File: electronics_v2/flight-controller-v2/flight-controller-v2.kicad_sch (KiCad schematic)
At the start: 4 parts

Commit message: develop Hall velocity sense circuit
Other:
- sheet sensors ports: added HALL_IC; removed none
- note added: "zapasowy uart zapasowe gpio peryferium ETR/IC więcej ledów"
- note removed: "zapasowy uart zapasowe gpio hal + komperator + peryferium więcej ledów"
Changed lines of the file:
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@@
     (effects (font (size 1.27 1.27)) (justify left bottom))
   )
-  (text "zapasowy uart\nzapasowe gpio\n\nhal + komperator + peryferium\n\nwięcej ledów"
+  (text "zapasowy uart\nzapasowe gpio\n\nperyferium ETR/IC\n\nwięcej ledów"
     (at 133.35 62.23 0)
     (effects (font (size 1.27 1.27)) (justify left bottom))
@@
       (effects (font (size 1.27 1.27)) (justify left))
     )
+    (pin "HALL_IC" output (at 173.99 80.01 180)
+      (effects (font (size 1.27 1.27)) (justify left))
+    )
   )
   (sheet_instances
@@
       (reference "#PWR?") (unit 1) (value "+3.3V") (footprint "")
     )
+    (path "/d1a36df1-5a51-492c-9a9f-effbb0092bf0/20096bc6-a896-4154-a5ab-fade95ff73b7"
+      (reference "#PWR?") (unit 1) (value "+3.3V") (footprint "")
+    )
     (path "/149c5d61-baf1-4212-9ad9-405f30b44c95/21926d48-3026-48c6-8cdc-e5929b77d4ef"
       (reference "#PWR?") (unit 1) (value "+3.3V") (footprint "")
@@
       (reference "#PWR?") (unit 1) (value "+3.3V") (footprint "")
     )
+    (path "/d1a36df1-5a51-492c-9a9f-effbb0092bf0/29cb5c89-06d9-4006-9814-2a4880c1b819"
+      (reference "#PWR?") (unit 1) (value "+3.3V") (footprint "")
+    )
     (path "/149c5d61-baf1-4212-9ad9-405f30b44c95/2ece62cc-6dc1-45d6-8c6e-3513ac4effd1"
       (reference "#PWR?") (unit 1) (value "GND") (footprint "")
@@
       (reference "#PWR?") (unit 1) (value "GND") (footprint "")
     )
+    (path "/d1a36df1-5a51-492c-9a9f-effbb0092bf0/377607cf-041d-4d18-b109-f0b4ec6f876a"
+      (reference "#PWR?") (unit 1) (value "+3.3V") (footprint "")
+    )
     (path "/d1a36df1-5a51-492c-9a9f-effbb0092bf0/38858d2f-1770-4298-a4e3-3f81257a2d0d"
       (reference "#PWR?") (unit 1) (value "+3.3V") (footprint "")
@@
       (reference "#PWR?") (unit 1) (value "+3.3V") (footprint "")
     )
+    (path "/d1a36df1-5a51-492c-9a9f-effbb0092bf0/464ba5a5-93fd-41e6-84ea-ede7d22b71fe"
+      (reference "#PWR?") (unit 1) (value "+3.3V") (footprint "")
+    )
     (path "/149c5d61-baf1-4212-9ad9-405f30b44c95/4a7c64b9-2073-446f-bf89-c69240feb67e"
       (reference "#PWR?") (unit 1) (value "GND") (footprint "")
@@
       (reference "#PWR?") (unit 1) (value "GND") (footprint "")
     )
+    (path "/d1a36df1-5a51-492c-9a9f-effbb0092bf0/522011a0-f0d8-4ba7-9e6f-5ff9a33e38b1"
+      (reference "#PWR?") (unit 1) (value "GND") (footprint "")
+    )
     (path "/d1a36df1-5a51-492c-9a9f-effbb0092bf0/5d48f08e-8f67-44af-a8a7-923a56ca9605"
+      (reference "#PWR?") (unit 1) (value "GND") (footprint "")
+    )
+    (path "/d1a36df1-5a51-492c-9a9f-effbb0092bf0/5effa745-d9f7-4e5b-b649-a19cf3afaa93"
       (reference "#PWR?") (unit 1) (value "GND") (footprint "")
     )
@@
       (reference "#PWR?") (unit 1) (value "GND") (footprint "")
     )
+    (path "/d1a36df1-5a51-492c-9a9f-effbb0092bf0/7e636a41-d55a-49c8-968f-3c89c4240551"
+      (reference "#PWR?") (unit 1) (value "GND") (footprint "")
+    )
     (path "/d1a36df1-5a51-492c-9a9f-effbb0092bf0/804a568e-50ef-433e-82e3-153830ebc752"
       (reference "#PWR?") (unit 1) (value "+3.3V") (footprint "")
@@
       (reference "#PWR?") (unit 1) (value "GND") (footprint "")
     )
+    (path "/d1a36df1-5a51-492c-9a9f-effbb0092bf0/a8c79890-aa93-491d-ab62-bc26d8e4490a"
+      (reference "#PWR?") (unit 1) (value "+3.3V") (footprint "")
+    )
     (path "/149c5d61-baf1-4212-9ad9-405f30b44c95/adb971b1-c38a-40db-9d84-a54e74a80d7a"
       (reference "#PWR?") (unit 1) (value "GND") (footprint "")
@@
     )
     (path "/149c5d61-baf1-4212-9ad9-405f30b44c95/baced8f9-e45b-4a13-a99a-093e8b3c04c1"
+      (reference "#PWR?") (unit 1) (value "GND") (footprint "")
+    )
+    (path "/d1a36df1-5a51-492c-9a9f-effbb0092bf0/c19aa58d-3819-46d5-89f6-f3e3056154ed"
       (reference "#PWR?") (unit 1) (value "GND") (footprint "")
     )
@@
       (reference "C?") (unit 1) (value "100n") (footprint "Capacitor_SMD:C_0603_1608Metric")
     )
+    (path "/d1a36df1-5a51-492c-9a9f-effbb0092bf0/d8f47615-6c6f-48d8-b535-4139ea3ff8a5"
+      (reference "C?") (unit 1) (value "100n") (footprint "Capacitor_SMD:C_0603_1608Metric")
+    )
     (path "/815a0815-7930-45ec-8d6e-dc110f979c75/f66445a3-dc52-405e-883b-923ec876e758"
       (reference "C?") (unit 1) (value "4u7") (footprint "Capacitor_Tantalum_SMD:CP_EIA-3216-18_Kemet-A")
@@
       (reference "D?") (unit 1) (value "BAT54S") (footprint "Package_TO_SOT_SMD:SOT-23")
     )
+    (path "/d1a36df1-5a51-492c-9a9f-effbb0092bf0/7f2d8310-974e-475b-bba2-aab509d13a3e"
+      (reference "D?") (unit 1) (value "LED") (footprint "LED_SMD:LED_0603_1608Metric")
+    )
     (path "/149c5d61-baf1-4212-9ad9-405f30b44c95/856db4e8-55ec-4206-89a5-cc9c66c03311"
       (reference "D?") (unit 1) (value "LED") (footprint "LED_SMD:LED_0603_1608Metric")
@@
       (reference "J?") (unit 1) (value "Conn_01x05") (footprint "goose:tht_pin_01x05")
     )
+    (path "/d1a36df1-5a51-492c-9a9f-effbb0092bf0/d28ebe5c-8369-47bf-abbe-3c33dc1af511"
+      (reference "J?") (unit 1) (value "Conn_01x03") (footprint "")
+    )
     (path "/149c5d61-baf1-4212-9ad9-405f30b44c95/d8cfee57-9cff-4276-ab5d-960c5e1d36df"
       (reference "J?") (unit 1) (value "Conn_02x03_Odd_Even") (footprint "")
@@
       (reference "R?") (unit 1) (value "1k") (footprint "Resistor_SMD:R_0603_1608Metric")
     )
+    (path "/d1a36df1-5a51-492c-9a9f-effbb0092bf0/3545fb41-1577-4cf1-80c9-3dc6ab45168c"
+      (reference "R?") (unit 1) (value "100k") (footprint "")
+    )
     (path "/149c5d61-baf1-4212-9ad9-405f30b44c95/36330f42-b9c4-4ab6-b3cd-2de4751d63c1"
       (reference "R?") (unit 1) (value "4k7") (footprint "Resistor_SMD:R_0603_1608Metric")
@@
     (path "/149c5d61-baf1-4212-9ad9-405f30b44c95/3c7eae78-be5c-4aed-9220-5501a3a80feb"
       (reference "R?") (unit 1) (value "4k7") (footprint "Resistor_SMD:R_0603_1608Metric")
+    )
+    (path "/d1a36df1-5a51-492c-9a9f-effbb0092bf0/5461e9bd-af58-4d4c-9c5e-853f9e0ac171"
+      (reference "R?") (unit 1) (value "1k") (footprint "Resistor_SMD:R_0603_1608Metric")
     )
     (path "/149c5d61-baf1-4212-9ad9-405f30b44c95/5abf4f3a-f370-40ce-a4a2-3f15d222669d"
       (reference "R?") (unit 1) (value "470k") (footprint "Resistor_SMD:R_0603_1608Metric")
     )
+    (path "/d1a36df1-5a51-492c-9a9f-effbb0092bf0/701a0902-e3fc-43c6-9811-ce7aecf33d86"
+      (reference "R?") (unit 1) (value "100k") (footprint "")
+    )
+    (path "/d1a36df1-5a51-492c-9a9f-effbb0092bf0/71e4532c-0456-4789-9a2a-aa4a489625de"
+      (reference "R?") (unit 1) (value "100k") (footprint "")
+    )
     (path "/149c5d61-baf1-4212-9ad9-405f30b44c95/735c5b7d-79c8-43ca-a41f-ca12ac9ea5af"
       (reference "R?") (unit 1) (value "4k7") (footprint "Resistor_SMD:R_0603_1608Metric")
+    )
+    (path "/d1a36df1-5a51-492c-9a9f-effbb0092bf0/7584f1ef-8386-4964-a02e-6599a7969b57"
+      (reference "R?") (unit 1) (value "1k5") (footprint "")
     )
     (path "/149c5d61-baf1-4212-9ad9-405f30b44c95/80fde87f-c9a8-4f4d-99bf-276acbefe674"
@@
       (reference "R?") (unit 1) (value "4k7") (footprint "Resistor_SMD:R_0603_1608Metric")
     )
+    (path "/d1a36df1-5a51-492c-9a9f-effbb0092bf0/c33467df-6a86-47e2-9894-be86d4d5b478"
+      (reference "R?") (unit 1) (value "100k") (footprint "Resistor_SMD:R_0603_1608Metric")
+    )
     (path "/815a0815-7930-45ec-8d6e-dc110f979c75/fc8307e0-8cda-401f-af73-afce55d85bbe"
       (reference "R?") (unit 1) (value "16k") (footprint "Resistor_SMD:R_0603_1608Metric")
@@
       (reference "SW?") (unit 1) (value "SW_Push") (footprint "Button_Switch_SMD:SW_Push_SPST_NO_Alps_SKRK")
     )
+    (path "/d1a36df1-5a51-492c-9a9f-effbb0092bf0/3fa1556d-ab9f-4dbd-96b1-a5804892d512"
+      (reference "U?") (unit 1) (value "LM393") (footprint "")
+    )
     (path "/d1a36df1-5a51-492c-9a9f-effbb0092bf0/81f6b743-8485-4f33-aa87-0cbd561a9277"
       (reference "U?") (unit 1) (value "BMP280") (footprint "goose:bmp280_hand_solder")
@@
       (reference "U?") (unit 1) (value "ESP-12E") (footprint "RF_Module:ESP-12E")
     )
+    (path "/d1a36df1-5a51-492c-9a9f-effbb0092bf0/65d088a9-1852-47d0-99be-e876bf4b7b24"
+      (reference "U?") (unit 3) (value "LM393") (footprint "")
+    )
     (path "/149c5d61-baf1-4212-9ad9-405f30b44c95/18886200-e5d2-4c7a-ae27-0137a2c1162c"

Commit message: FC scheme complete
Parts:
- H1, H2, H3, H4: renamed from H?; footprint (none) -> MountingHole:MountingHole_3.2mm_M3_Pad_Via
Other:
- sheet sensors ports: added HALL; removed HALL_IC
- sheet ucontroller ports: added HALL_TIM2_ETR; removed none
- note removed: "zapasowy uart zapasowe gpio peryferium ETR/IC więcej ledów"

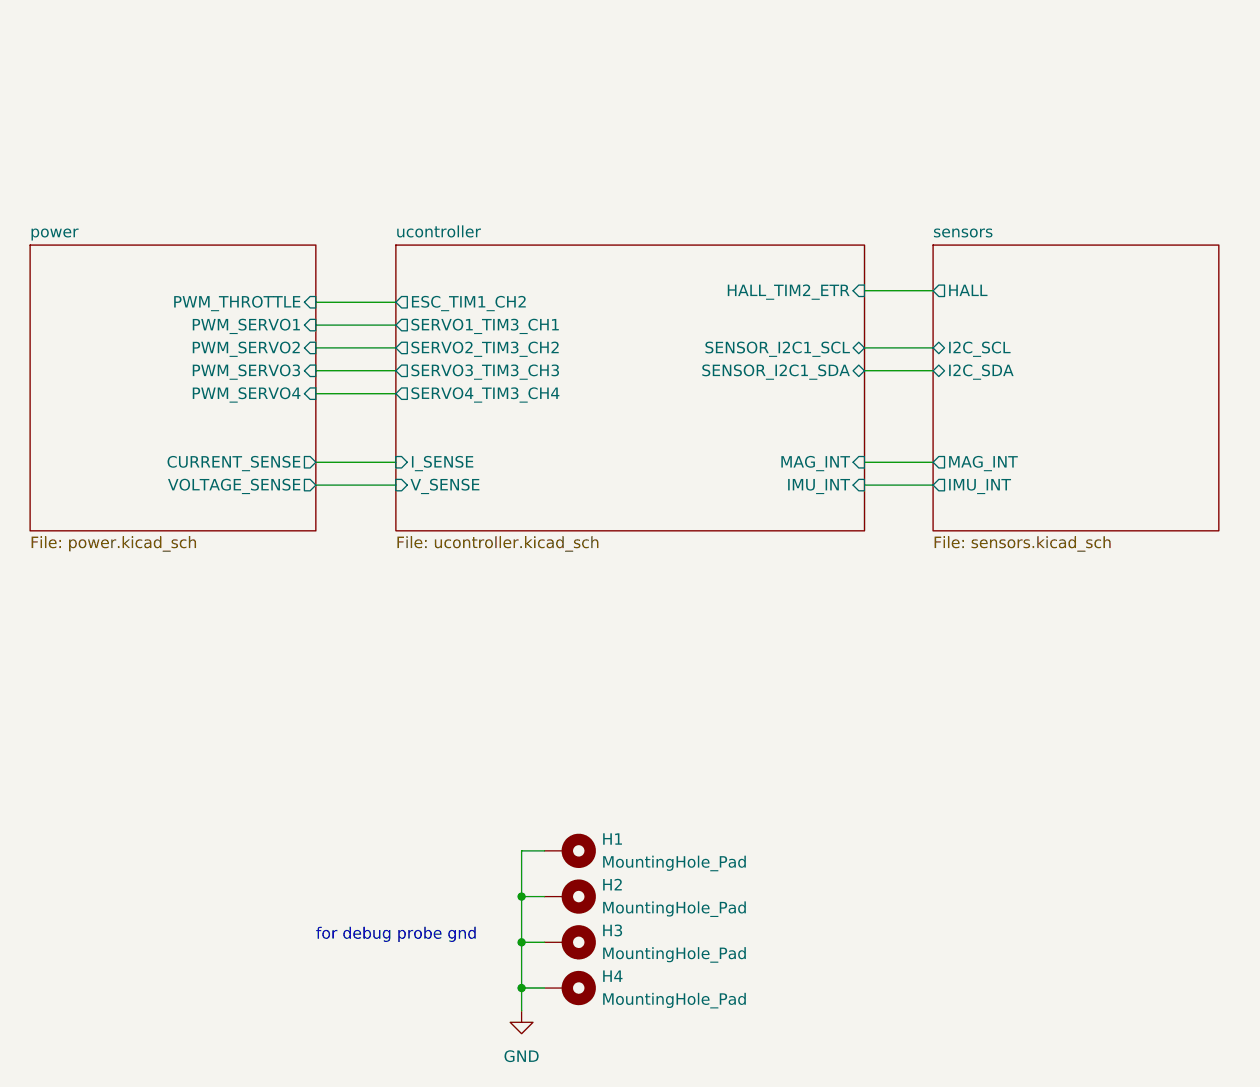
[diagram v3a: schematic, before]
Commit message: edge XT60 connector & INA226 I2C measurement
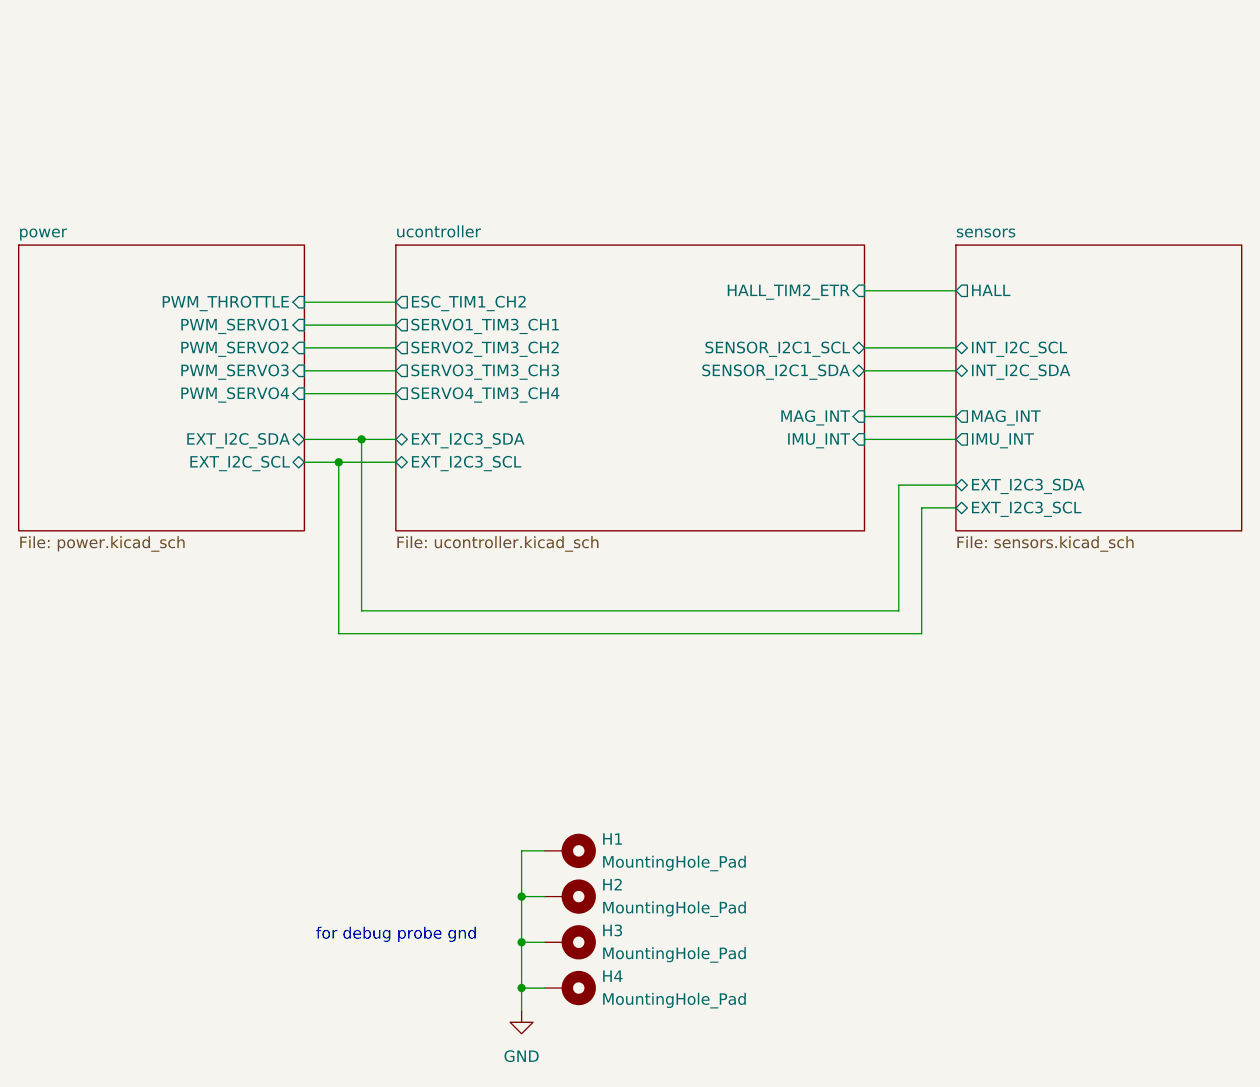
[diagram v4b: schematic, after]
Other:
- sheet power ports: added EXT_I2C_SCL, EXT_I2C_SDA; removed CURRENT_SENSE, VOLTAGE_SENSE
- sheet sensors ports: added EXT_I2C3_SCL, EXT_I2C3_SDA, INT_I2C_SCL, INT_I2C_SDA; removed I2C_SCL, I2C_SDA
- sheet ucontroller ports: added EXT_I2C3_SCL, EXT_I2C3_SDA; removed I_SENSE, V_SENSE

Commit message: move PLI to FC
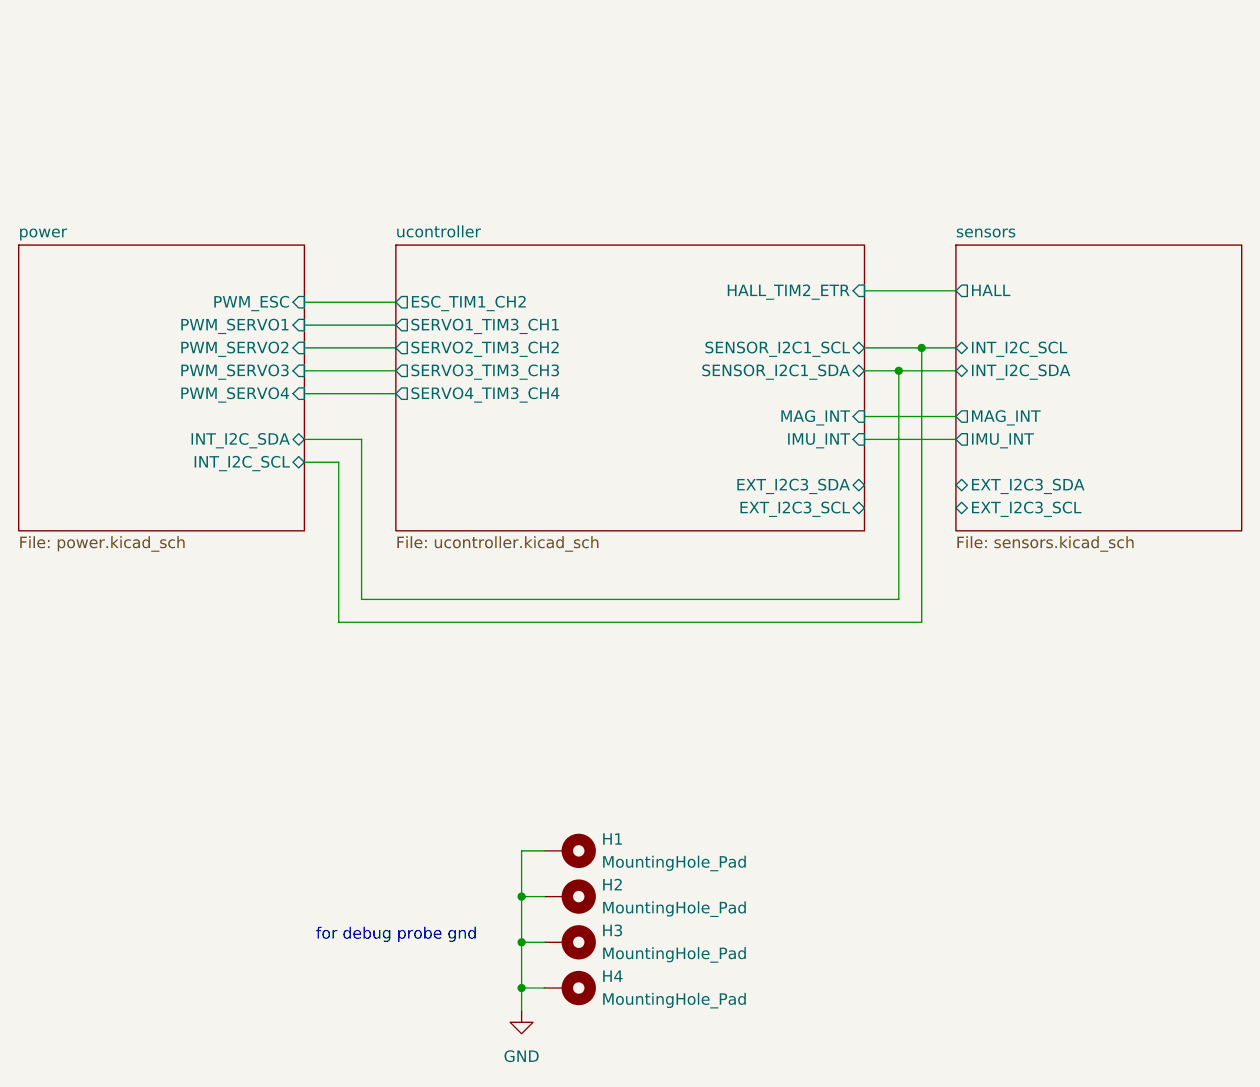
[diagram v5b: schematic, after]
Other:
- sheet power ports: added INT_I2C_SCL, INT_I2C_SDA, PWM_ESC; removed EXT_I2C_SCL, EXT_I2C_SDA, PWM_THROTTLE

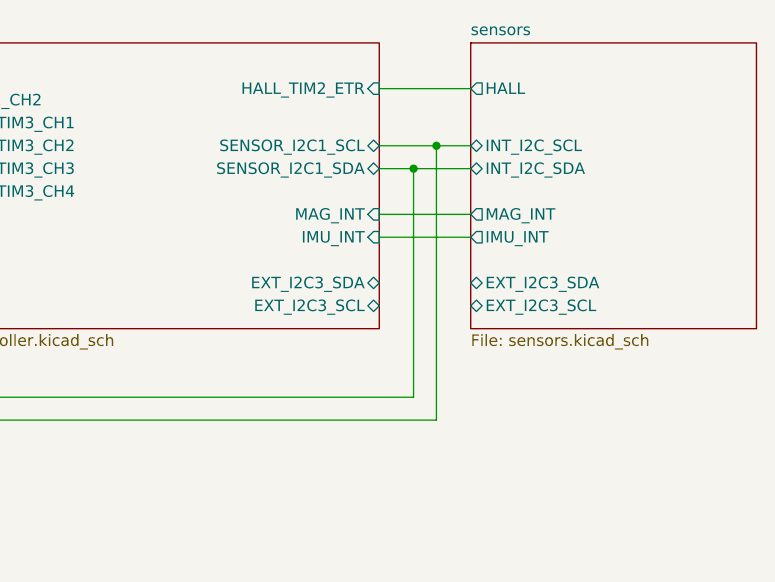
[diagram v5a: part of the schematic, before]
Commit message: fix route names
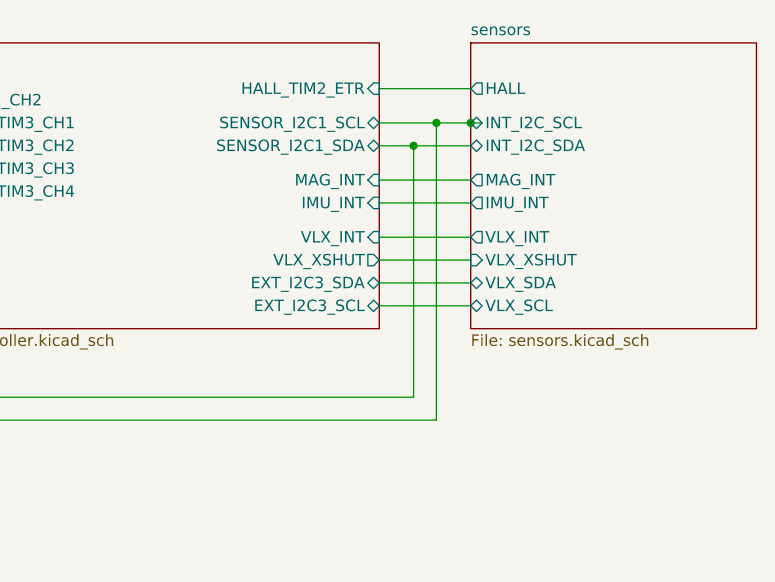
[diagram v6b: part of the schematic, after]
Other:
- sheet sensors ports: added VLX_INT, VLX_SCL, VLX_SDA, VLX_XSHUT; removed EXT_I2C3_SCL, EXT_I2C3_SDA
- sheet ucontroller ports: added VLX_INT, VLX_XSHUT; removed none
